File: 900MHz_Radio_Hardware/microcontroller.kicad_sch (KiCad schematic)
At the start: 3 parts, among them J1 RJ45_LED_Shielded, U2 Teensy4.1_DEV-16771

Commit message: Replaced oscillator Tune circuit
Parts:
- added SW2: SW_SPDT, symbol Switch:SW_SPDT
- added U7: MCP4725xxx-xCH, Package_TO_SOT_SMD:SOT-23-6, symbol Analog_DAC:MCP4725xxx-xCH
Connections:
- net GNDPWR: now also SW2.3 (C), U7.3 (VDD)
- net at U2.18 (A4): now also U7.4 (SDA)
- net at U2.19 (A5): now also U7.5 (SCL)
- net +3V3: now reaches U2.3.3V_1 (3.3V), U2.3.3V_2 (3.3V), U2.3.3V_3 (3.3V)
- net +3V3: now also SW2.1 (A), U7.2 (VSS)
- net OSC_CTL_A: no longer names the net of U2.23 (A9)
- net OSC_CTL_B: no longer names the net of U2.24 (A10)
- net OSC_CTL_C: no longer names the net of U2.25 (A11)
- net OSC_ENB renamed MCU_OSC_ENB
- new net: SW2.2 (B), U7.6 (A0)
- new net MCU_OSC_CTL: U7.1 (VOUT)
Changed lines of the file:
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@@
   (junction (at 237.49 74.93) (diameter 0) (color 0 0 0 0)
+  )
+  (junction (at 60.96 105.41) (diameter 0) (color 0 0 0 0)
+  )
+  (junction (at 60.96 130.81) (diameter 0) (color 0 0 0 0)
   )
   (junction (at 237.49 67.31) (diameter 0) (color 0 0 0 0)
@@
     (stroke (width 0) (type default))
   )
+  (wire (pts (xy 60.96 105.41) (xy 87.63 105.41))
+    (stroke (width 0) (type default))
+  )
   (wire (pts (xy 171.45 138.43) (xy 171.45 144.78))
     (stroke (width 0) (type default))
   )
+  (wire (pts (xy 72.39 125.73) (xy 127 125.73))
+    (stroke (width 0) (type default))
+  )
+  (wire (pts (xy 71.12 120.65) (xy 72.39 120.65))
+    (stroke (width 0) (type default))
+  )
   (wire (pts (xy 222.25 64.77) (xy 240.03 64.77))
     (stroke (width 0) (type default))
@@
     (stroke (width 0) (type default))
   )
-  (wire (pts (xy 167.64 130.81) (xy 172.72 130.81))
+  (wire (pts (xy 87.63 113.03) (xy 85.09 113.03))
     (stroke (width 0) (type default))
   )
@@
     (stroke (width 0) (type default))
   )
+  (wire (pts (xy 87.63 130.81) (xy 60.96 130.81))
+    (stroke (width 0) (type default))
+  )
   (wire (pts (xy 260.35 74.93) (xy 261.62 74.93))
     (stroke (width 0) (type default))
@@
     (stroke (width 0) (type default))
   )
+  (wire (pts (xy 60.96 105.41) (xy 60.96 110.49))
+    (stroke (width 0) (type default))
+  )
   (wire (pts (xy 224.79 67.31) (xy 237.49 67.31))
     (stroke (width 0) (type default))
@@
     (stroke (width 0) (type default))
   )
+  (wire (pts (xy 60.96 102.87) (xy 60.96 105.41))
+    (stroke (width 0) (type default))
+  )
   (bus (pts (xy 219.71 53.34) (xy 219.71 54.61))
     (stroke (width 0) (type default))
@@
     (stroke (width 0) (type default))
   )
-  (wire (pts (xy 167.64 133.35) (xy 172.72 133.35))
+  (wire (pts (xy 60.96 130.81) (xy 60.96 133.35))
     (stroke (width 0) (type default))
   )
@@
     (stroke (width 0) (type default))
   )
+  (wire (pts (xy 170.18 46.99) (xy 167.64 46.99))
+    (stroke (width 0) (type default))
+  )
+  (wire (pts (xy 72.39 120.65) (xy 72.39 125.73))
+    (stroke (width 0) (type default))
+  )
+  (wire (pts (xy 71.12 118.11) (xy 74.93 118.11))
+    (stroke (width 0) (type default))
+  )
   (wire (pts (xy 167.64 67.31) (xy 177.8 67.31))
     (stroke (width 0) (type default))
@@
     (stroke (width 0) (type default))
   )
+  (wire (pts (xy 170.18 44.45) (xy 170.18 46.99))
+    (stroke (width 0) (type default))
+  )
   (wire (pts (xy 264.16 72.39) (xy 264.16 83.82))
     (stroke (width 0) (type default))
   )
-  (wire (pts (xy 167.64 128.27) (xy 172.72 128.27))
-    (stroke (width 0) (type default))
-  )
   (wire (pts (xy 167.64 64.77) (xy 177.8 64.77))
     (stroke (width 0) (type default))
@@
     (stroke (width 0) (type default))
   )
+  (wire (pts (xy 60.96 125.73) (xy 60.96 130.81))
+    (stroke (width 0) (type default))
+  )
+  (wire (pts (xy 85.09 118.11) (xy 87.63 118.11))
+    (stroke (width 0) (type default))
+  )
   (wire (pts (xy 222.25 62.23) (xy 240.03 62.23))
     (stroke (width 0) (type default))
@@
     (stroke (width 0) (type default))
   )
+  (wire (pts (xy 71.12 115.57) (xy 74.93 115.57))
+    (stroke (width 0) (type default))
+  )
   (wire (pts (xy 222.25 69.85) (xy 240.03 69.85))
     (stroke (width 0) (type default))
@@
     (stroke (width 0) (type default))
   )
+  (wire (pts (xy 45.72 118.11) (xy 50.8 118.11))
+    (stroke (width 0) (type default))
+  )
   (bus (pts (xy 219.71 54.61) (xy 219.71 59.69))
     (stroke (width 0) (type default))
@@
     (stroke (width 0) (type default))
   )
+  (wire (pts (xy 87.63 118.11) (xy 87.63 130.81))
+    (stroke (width 0) (type default))
+  )
+  (wire (pts (xy 74.93 118.11) (xy 74.93 123.19))
+    (stroke (width 0) (type default))
+  )
   (wire (pts (xy 123.19 57.15) (xy 127 57.15))
     (stroke (width 0) (type default))
@@
     (stroke (width 0) (type default))
   )
+  (wire (pts (xy 87.63 105.41) (xy 87.63 113.03))
+    (stroke (width 0) (type default))
+  )
+  (wire (pts (xy 74.93 123.19) (xy 127 123.19))
+    (stroke (width 0) (type default))
+  )
   (wire (pts (xy 231.14 74.93) (xy 224.79 74.93))
     (stroke (width 0) (type default))
@@
     (effects (font (size 1.27 1.27)) (justify left bottom))
   )
-  (hierarchical_label "OSC_ENB" (shape output) (at 124.46 95.25 180) (fields_autoplaced)
+  (hierarchical_label "MCU_OSC_ENB" (shape output) (at 124.46 95.25 180) (fields_autoplaced)
     (effects (font (size 1.27 1.27)) (justify right))
   )
-  (hierarchical_label "OSC_CTL_B" (shape output) (at 172.72 130.81 0) (fields_autoplaced)
-    (effects (font (size 1.27 1.27)) (justify left))
-  )
-  (hierarchical_label "OSC_CTL_C" (shape output) (at 172.72 128.27 0) (fields_autoplaced)
-    (effects (font (size 1.27 1.27)) (justify left))
-  )
-  (hierarchical_label "OSC_CTL_A" (shape output) (at 172.72 133.35 0) (fields_autoplaced)
-    (effects (font (size 1.27 1.27)) (justify left))
+  (hierarchical_label "MCU_OSC_CTL" (shape output) (at 45.72 118.11 180) (fields_autoplaced)
+    (effects (font (size 1.27 1.27)) (justify right))
+  )
+  (symbol (lib_id "Switch:SW_SPDT") (at 80.01 115.57 0) (unit 1)
+    (in_bom yes) (on_board yes) (dnp no) (fields_autoplaced)
+    (property "Reference" "SW2" (at 80.01 107.95 0)
+      (effects (font (size 1.27 1.27)))
+    )
+    (property "Value" "SW_SPDT" (at 80.01 110.49 0)
+      (effects (font (size 1.27 1.27)))
+    )
+    (property "Footprint" "" (at 80.01 115.57 0)
+      (effects (font (size 1.27 1.27)) hide)
+    )
+    (property "Datasheet" "~" (at 80.01 115.57 0)
+      (effects (font (size 1.27 1.27)) hide)
+    )
+    (pin "1")
+    (pin "2")
+    (pin "3")
+    (instances
+      (project "900MHz_Radio_Hardware"
+        (path "/8d477a51-3dbb-4c04-84c7-90186d141eda/fd7e5d4a-4a71-414e-9993-037c48e39dc4"
+          (reference "SW2") (unit 1)
+        )
+      )
+    )
   )
   (symbol (lib_id "power:+5V") (at 123.19 53.34 0) (unit 1)
@@
         (path "/8d477a51-3dbb-4c04-84c7-90186d141eda/fd7e5d4a-4a71-414e-9993-037c48e39dc4"
           (reference "#PWR022") (unit 1)
+        )
+      )
+    )
+  )
+  (symbol (lib_id "power:GNDPWR") (at 60.96 133.35 0) (unit 1)
+    (in_bom yes) (on_board yes) (dnp no) (fields_autoplaced)
+    (property "Reference" "#PWR037" (at 60.96 138.43 0)
+      (effects (font (size 1.27 1.27)) hide)
+    )
+    (property "Value" "GNDPWR" (at 60.833 137.16 0)
+      (effects (font (size 1.27 1.27)))
+    )
+    (property "Footprint" "" (at 60.96 134.62 0)
+      (effects (font (size 1.27 1.27)) hide)
+    )
+    (property "Datasheet" "" (at 60.96 134.62 0)
+      (effects (font (size 1.27 1.27)) hide)
+    )
+    (pin "1")
+    (instances
+      (project "900MHz_Radio_Hardware"
+        (path "/8d477a51-3dbb-4c04-84c7-90186d141eda/fd7e5d4a-4a71-414e-9993-037c48e39dc4"
+          (reference "#PWR037") (unit 1)
         )
       )
@@
         (path "/8d477a51-3dbb-4c04-84c7-90186d141eda/fd7e5d4a-4a71-414e-9993-037c48e39dc4"
           (reference "C16") (unit 1)
+        )
+      )
+    )
+  )
+  (symbol (lib_id "power:+3V3") (at 60.96 102.87 0) (unit 1)
+    (in_bom yes) (on_board yes) (dnp no) (fields_autoplaced)
+    (property "Reference" "#PWR036" (at 60.96 106.68 0)
+      (effects (font (size 1.27 1.27)) hide)
+    )
+    (property "Value" "+3V3" (at 60.96 97.79 0)
+      (effects (font (size 1.27 1.27)))
+    )
+    (property "Footprint" "" (at 60.96 102.87 0)
+      (effects (font (size 1.27 1.27)) hide)
+    )
+    (property "Datasheet" "" (at 60.96 102.87 0)
+      (effects (font (size 1.27 1.27)) hide)
+    )
+    (pin "1")
+    (instances
+      (project "900MHz_Radio_Hardware"
+        (path "/8d477a51-3dbb-4c04-84c7-90186d141eda/fd7e5d4a-4a71-414e-9993-037c48e39dc4"
+          (reference "#PWR036") (unit 1)
         )
       )
@@
         )
       )
+    )
+  )
+  (symbol (lib_id "power:+3V3") (at 170.18 44.45 0) (unit 1)
+    (in_bom yes) (on_board yes) (dnp no) (fields_autoplaced)
+    (property "Reference" "#PWR010" (at 170.18 48.26 0)
+      (effects (font (size 1.27 1.27)) hide)
+    )
+    (property "Value" "+3V3" (at 170.18 39.37 0)
+      (effects (font (size 1.27 1.27)))
+    )
+    (property "Footprint" "" (at 170.18 44.45 0)
+      (effects (font (size 1.27 1.27)) hide)
+    )
+    (property "Datasheet" "" (at 170.18 44.45 0)
+      (effects (font (size 1.27 1.27)) hide)
+    )
+    (pin "1")
+    (instances
+      (project "900MHz_Radio_Hardware"
+        (path "/8d477a51-3dbb-4c04-84c7-90186d141eda/fd7e5d4a-4a71-414e-9993-037c48e39dc4"
+          (reference "#PWR010") (unit 1)
+        )
+      )
+    )
+  )
+  (symbol (lib_id "Analog_DAC:MCP4725xxx-xCH") (at 60.96 118.11 180) (unit 1)
+    (in_bom yes) (on_board yes) (dnp no)
+    (property "Reference" "U7" (at 43.18 124.46 0)
+      (effects (font (size 1.27 1.27)))
+    )
+    (property "Value" "MCP4725xxx-xCH" (at 43.18 121.92 0)
+      (effects (font (size 1.27 1.27)))
+    )
+    (property "Footprint" "Package_TO_SOT_SMD:SOT-23-6" (at 60.96 111.76 0)
+      (effects (font (size 1.27 1.27)) hide)
+    )
+    (property "Datasheet" "http://ww1.microchip.com/downloads/en/DeviceDoc/22039d.pdf" (at 60.96 118.11 0)
+      (effects (font (size 1.27 1.27)) hide)
+    )
+    (pin "1")
+    (pin "2")
+    (pin "3")
+    (pin "4")
+    (pin "5")
+    (pin "6")
+    (instances
+      (project "900MHz_Radio_Hardware"
+        (path "/8d477a51-3dbb-4c04-84c7-90186d141eda/fd7e5d4a-4a71-414e-9993-037c48e39dc4"
+          (reference "U7") (unit 1)
+        )
+      )

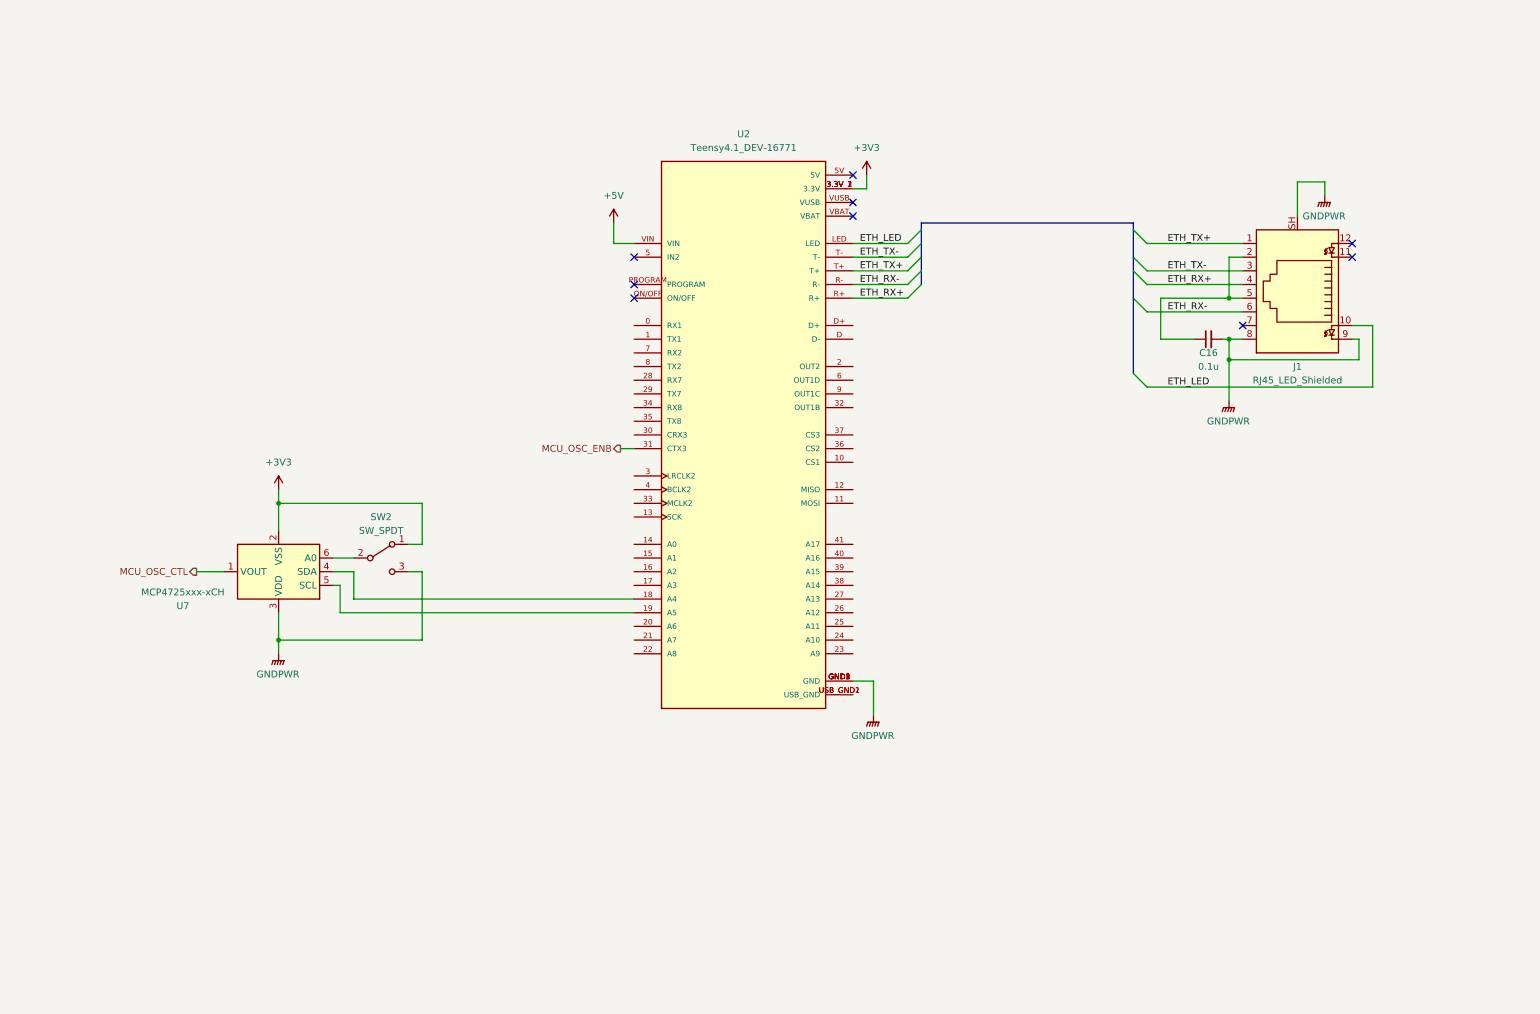
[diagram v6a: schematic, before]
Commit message: Cleaned up I2C connection
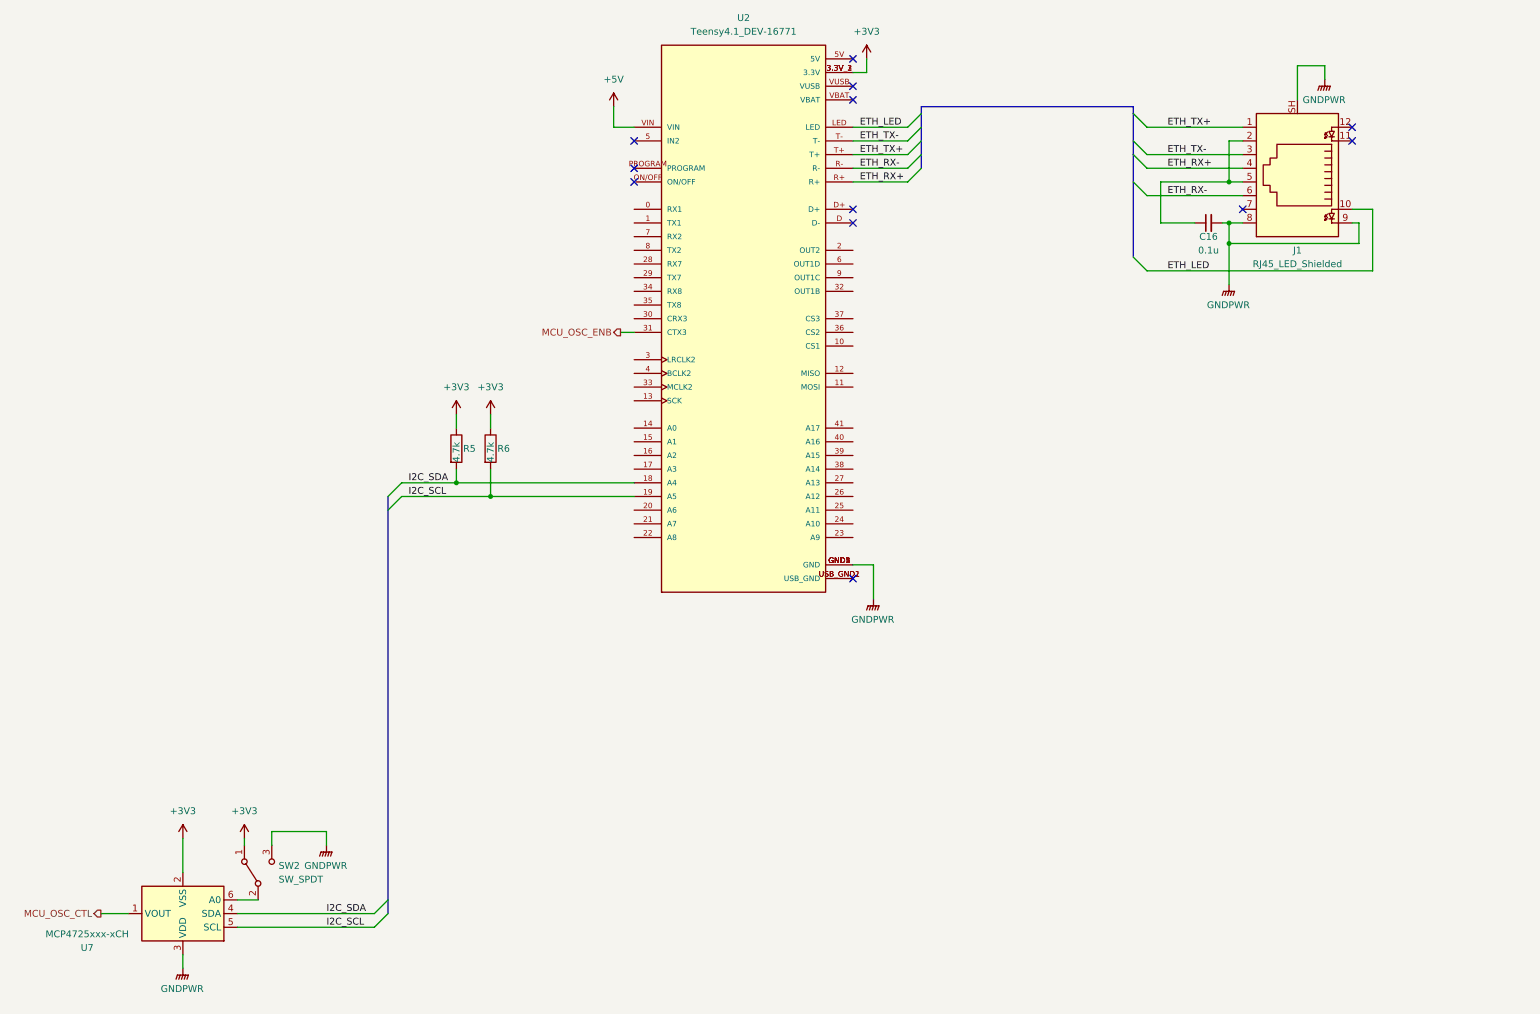
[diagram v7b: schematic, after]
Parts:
- added R5, R6: 4.7k, symbol Device:R
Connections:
- net +3V3: now also R5.1, R6.1
- net I2C_SDA: now reaches U2.18 (A4), U7.4 (SDA)
- net I2C_SDA: now also R5.2
- net I2C_SCL: now reaches U2.19 (A5), U7.5 (SCL)
- net I2C_SCL: now also R6.2
- no-connect marks 9 -> 12
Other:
- moved on the sheet: C16, J1, SW2, U2, U7

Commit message: Hardware for IQ signal synchronization
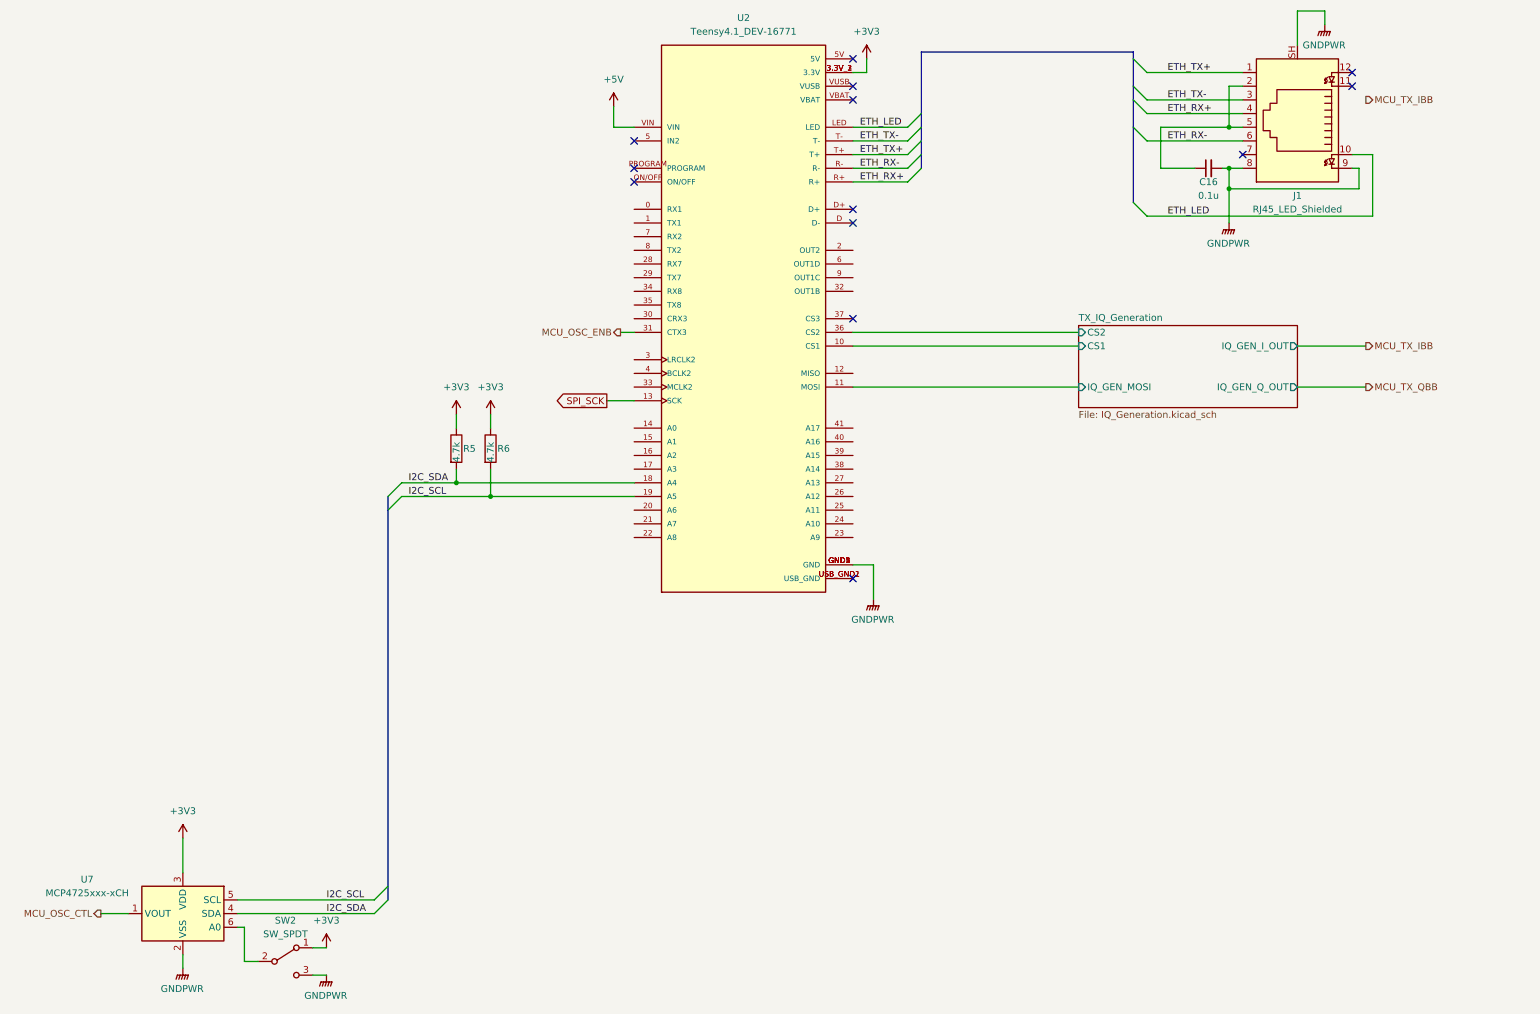
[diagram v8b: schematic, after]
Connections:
- net +3V3: now also U7.3 (VDD); no longer U7.2 (VSS)
- net GNDPWR: now also U7.2 (VSS); no longer U7.3 (VDD)
- net TX_IQ_Generation/CS1: now reaches U2.10 (CS1)
- net TX_IQ_Generation/IQ_GEN_MOSI: now reaches U2.11 (MOSI)
- net SPI_SCK: now reaches U2.13 (SCK)
- net TX_IQ_Generation/CS2: now reaches U2.36 (CS2)
- no-connect marks 12 -> 13
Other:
- added sheet TX_IQ_Generation (IQ_Generation.kicad_sch)
- moved on the sheet: C16, J1, U7
